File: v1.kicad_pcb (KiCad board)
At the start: 2 copper layers, 54 x 25.6 mm, 74 parts, among them J101 Conn_01x04, J102 Conn_01x04, J103 Conn_01x04, J104 Conn_01x04, J105 Conn_01x04, J106 K1X06, J107 FTDI, J108 ISP, J201 Conn_Coaxial, Q101 AO3400A, SW101 SW_Push, U101 ATmega328P-AU, U102 DS18B20, U103 PST61C24, U201 CC1101RGPR, Y101 8MHz, Y201 26MHz

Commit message: place Atmega328 circuits
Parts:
- removed BT102: 2AA, Battery:BatteryHolder_Keystone_2462_2xAA
- removed BT103: Coin, Battery:BatteryHolder_Keystone_3000_1x12mm
- moved J106 130.1 mm to (172.0, 157.2)
- moved J101 104.4 mm to (163.5, 111.8)
- moved R110 101.1 mm to (192.7, 126.2), turned to 270 degrees
- moved J102 100.4 mm to (176.6, 111.8)
- moved J107 100.2 mm to (163.9, 123.0), turned to 90 degrees
- moved J103 98.6 mm to (185.6, 112.0)
- moved Q101 98.5 mm to (191.7, 123.5), turned to 180 degrees
- moved C109 97.9 mm to (166.2, 120.7)
- moved R108 92.8 mm to (188.9, 120.9), turned to 180 degrees
- moved R109 92.6 mm to (191.9, 120.9), turned to 180 degrees
- moved U103 92.5 mm to (181.0, 118.9)
- moved R111 92.5 mm to (183.2, 118.8)
- moved C108 92.2 mm to (176.9, 131.7)
- moved C107 92.2 mm to (176.9, 129.8)
- moved Y101 92.2 mm to (174.5, 130.8)
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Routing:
- net +3V0: track 50.6 -> 15.6 mm, vias 0 -> 10
- net /A2: track 0.00 -> 18.2 mm, vias 0 -> 2
- net /D2: track 14.6 -> 32.2 mm, vias 0 -> 2
- net /D9: track 0.00 -> 12.7 mm, vias 0 -> 2
- net /MOSI: track 7.06 -> 19.5 mm, vias 0 -> 2
- net /D10: track 16.5 -> 27.3 mm
- net /D8: track 0.00 -> 9.08 mm, vias 0 -> 2
- net /MISO: track 8.93 -> 15.9 mm
- net /XTAL2: track 0.00 -> 6.54 mm
- net /A3: track 0.00 -> 6.17 mm
- net /A1: track 0.00 -> 5.75 mm
- net /XTAL1: track 0.00 -> 5.39 mm
- net /SCK: track 8.34 -> 13.4 mm
- net GND: track 47.5 -> 43.2 mm, vias 21 -> 33
- net Net-(C106-Pad1): track 0.00 -> 1.67 mm
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
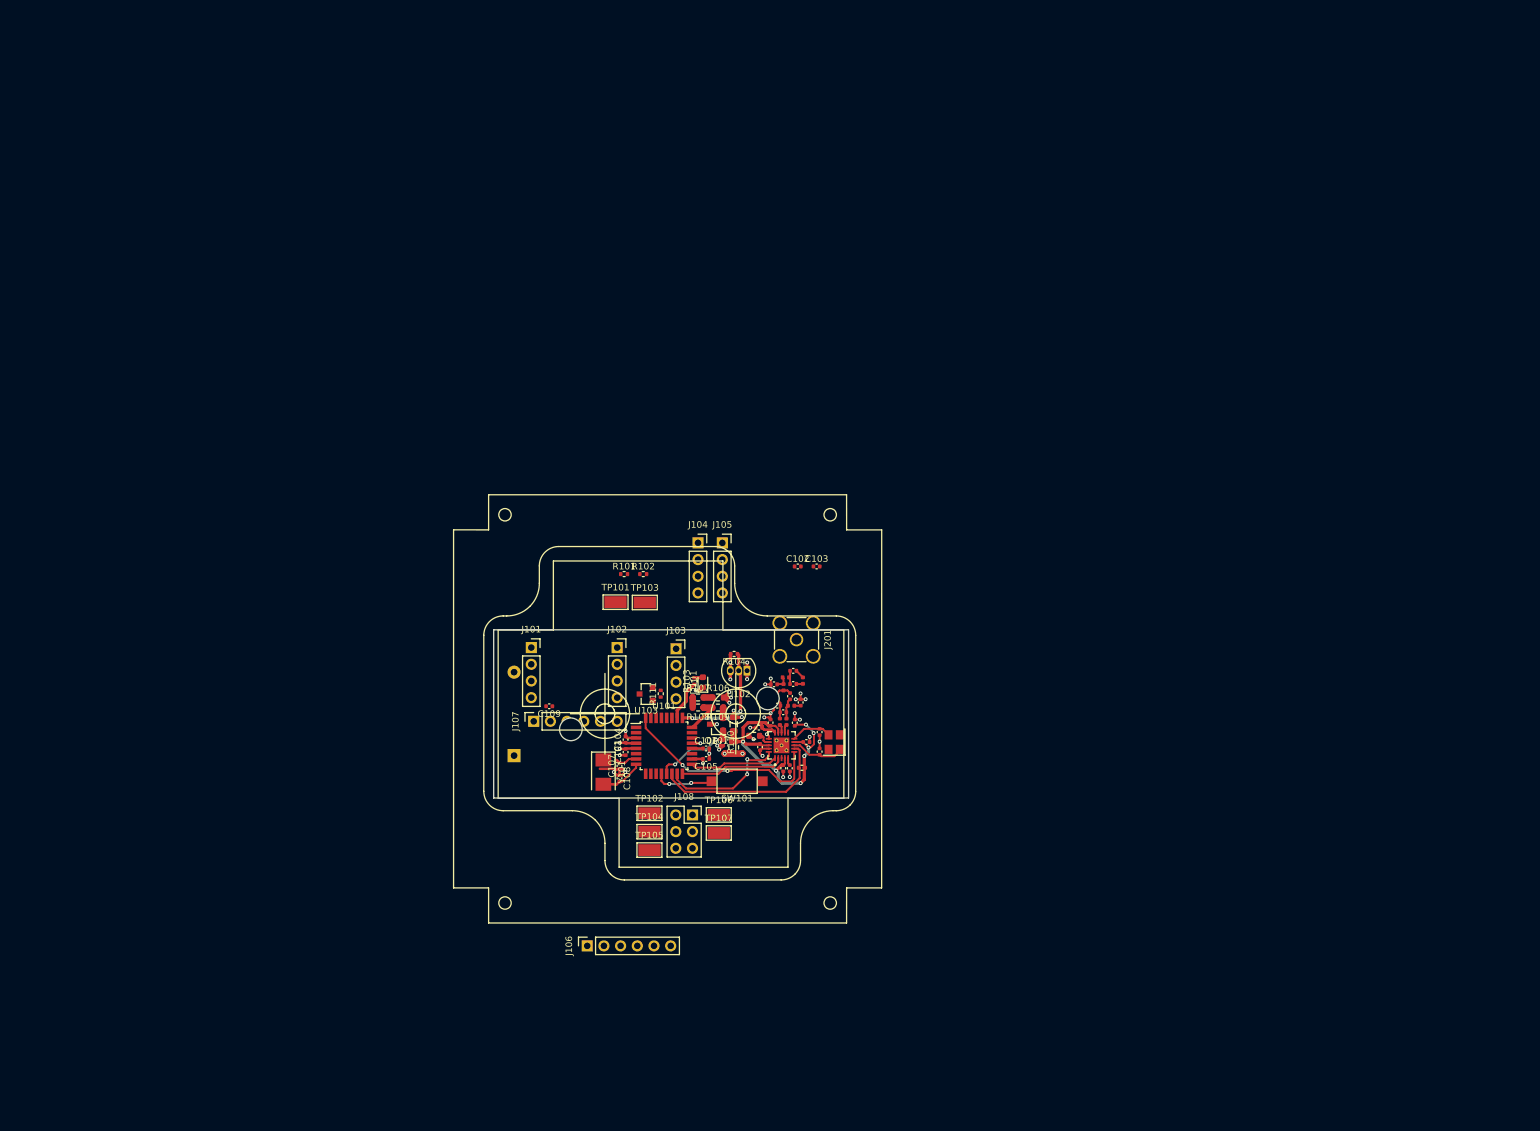
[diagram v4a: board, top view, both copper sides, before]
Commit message: adapt boards for kradex casings
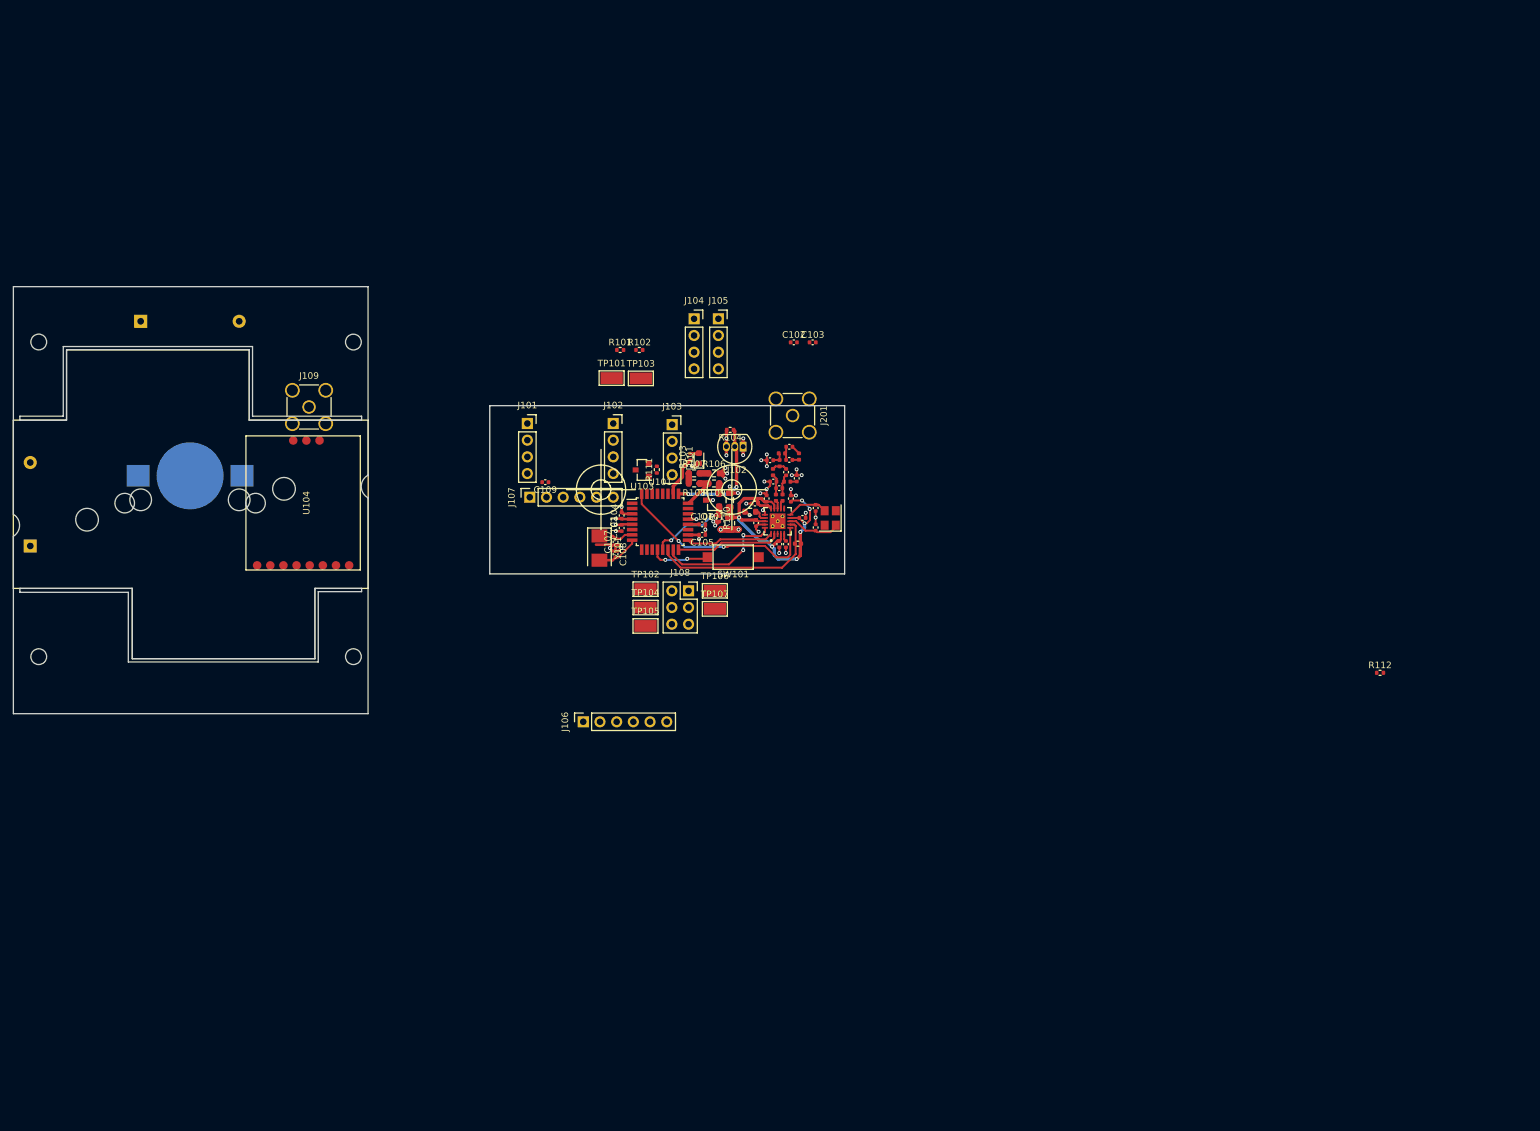
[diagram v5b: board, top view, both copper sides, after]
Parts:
- added BT102: 2AA, Battery:BatteryHolder_Keystone_2462_2xAA, B.Cu at (104.1, 62.2)
- added BT103: Coin, Battery:BatteryHolder_Keystone_3000_1x12mm, B.Cu at (111.6, 85.7)
- added J109: Conn_Coaxial, Connector_Coaxial:SMA_Amphenol_901-144_Vertical, F.Cu at (129.7, 75.2)
- added R112: 10k, Resistor_SMD:R_0402_1005Metric, F.Cu at (292.7, 115.7)
- added U104: CC1101-Ali, _project:CC1101-Ali, F.Cu at (128.8, 89.8)
- moved BT101 80.2 mm to (87.3, 96.3)
- moved C104 34.1 mm to (177.3, 91.7)
- moved C107 34.1 mm to (176.3, 95.7)
- moved C108 34.1 mm to (176.3, 97.6)
- moved C202 34.1 mm to (204.8, 92.1)
- moved C204 34.1 mm to (199.3, 89.1)
- moved C208 34.1 mm to (197.7, 92.8)
- moved C215 34.1 mm to (201.2, 87.5)
- moved C216 34.1 mm to (199.8, 83.3)
- moved C217 34.1 mm to (200.3, 86.5)
- moved J101 34.1 mm to (162.9, 77.7)
- moved J102 34.1 mm to (176.0, 77.7)
- moved J108 34.1 mm to (187.4, 103.2)
- moved L207 34.1 mm to (200.3, 85.1)
- moved R103 34.1 mm to (187.7, 82.8)
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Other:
- board size 54 x 25.6 mm -> 126.5 x 65 mm
- board text added: "Z123"
- board text added: "Z54"
